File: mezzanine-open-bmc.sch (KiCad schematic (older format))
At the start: 14 parts, among them CON1 USB-MINI-B, P1 CONN_02X20, P2 CONN_02X20, SW1 PWR, SW2 RST, U1 FT230XS

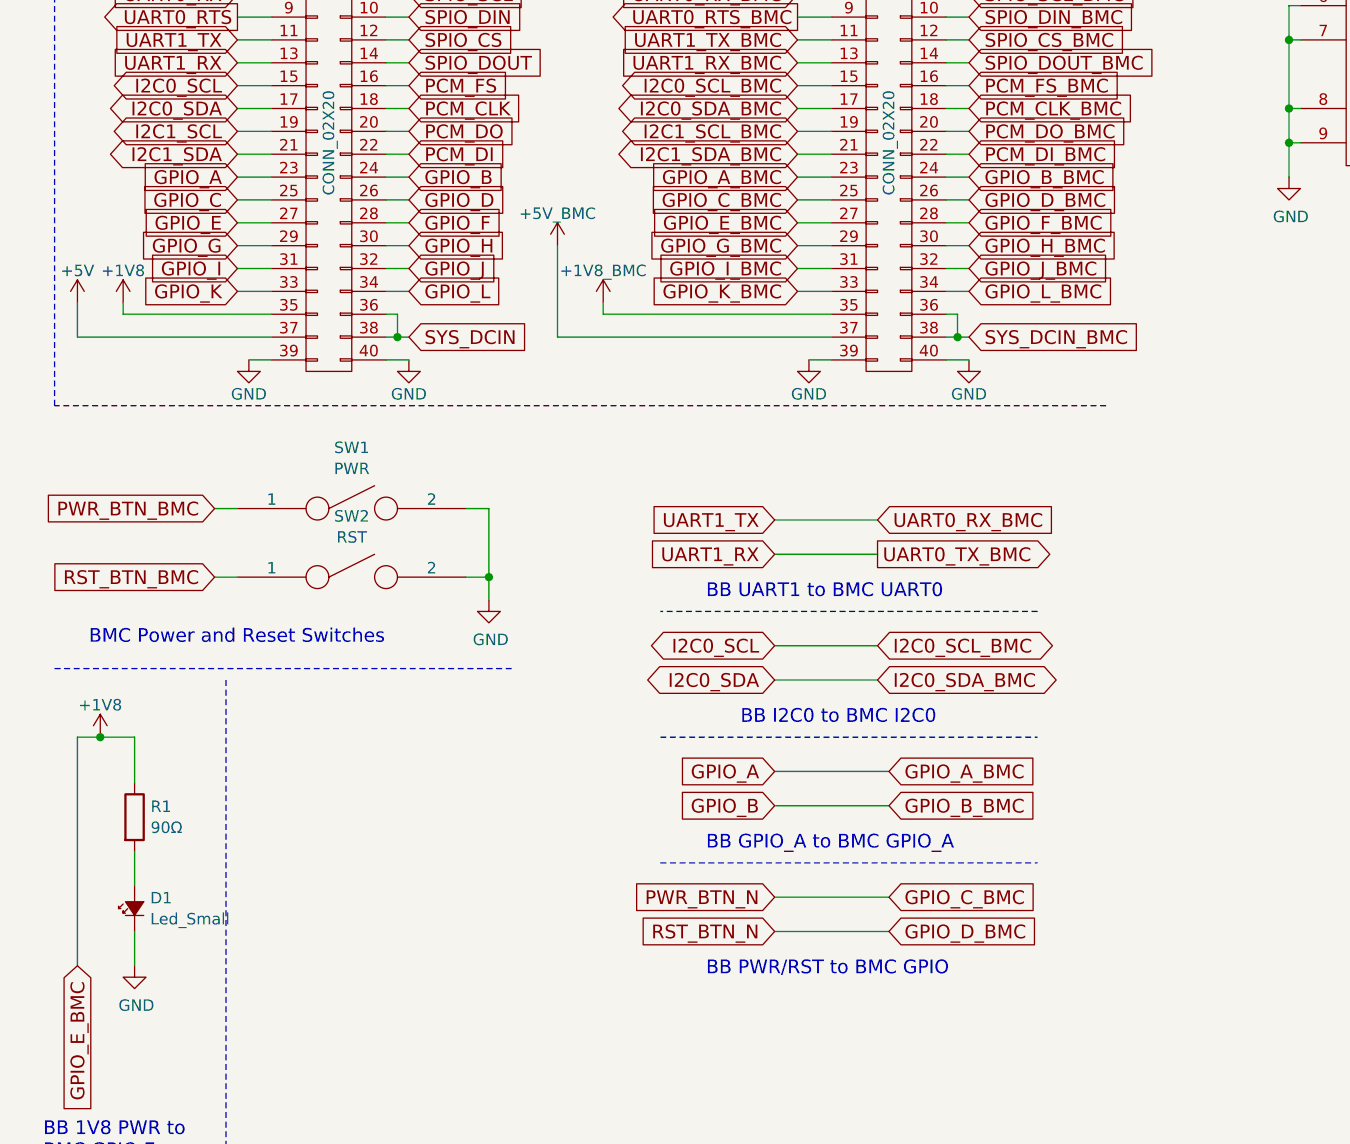
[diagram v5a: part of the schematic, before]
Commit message: Change Signal Names for GPIO_A/B BMC
Since GPIO_A and GPIO_B are to be connected on the BB & BMC pins,
the signal names have been renamed to match.

Signed-off-by: Sophie Haynes <sophie.haynes@linaro.org>
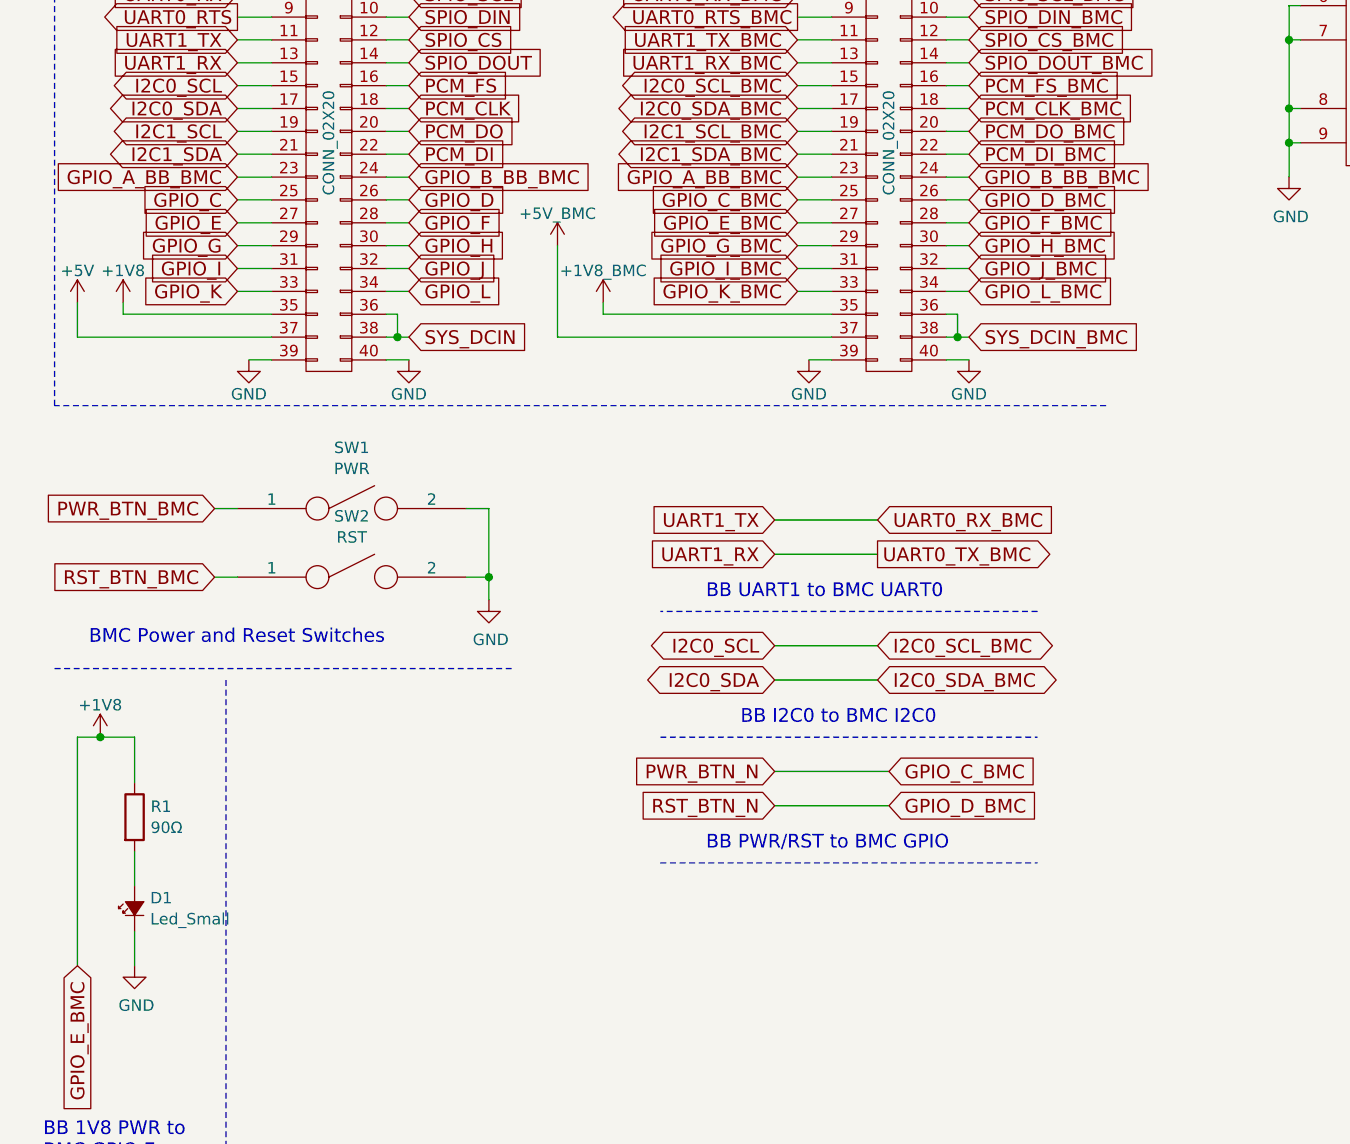
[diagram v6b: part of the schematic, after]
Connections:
- net GPIO_A renamed GPIO_A_BB_BMC
- net GPIO_B renamed GPIO_B_BB_BMC
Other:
- note removed: "BB GPIO_A to BMC GPIO_A"
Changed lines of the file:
@@
 I2C0_SCL_BMC
 Text GLabel 3950 2200 0    60   Input ~ 0
-GPIO_A_BMC
+GPIO_A_BB_BMC
 Text GLabel 3950 1400 0    60   Input ~ 0
 UART0_RX_BMC
@@
 UART1_RX_BMC
 Text GLabel 4700 2200 2    60   Input ~ 0
-GPIO_B_BMC
+GPIO_B_BB_BMC
 Text GLabel 4700 1400 2    60   Input ~ 0
 SPIO_SCL_BMC
@@
 UART0_CTS
 Text GLabel 1500 2200 0    60   Input ~ 0
-GPIO_A
+GPIO_A_BB_BMC
 Text GLabel 2250 2200 2    60   Input ~ 0
-GPIO_B
+GPIO_B_BB_BMC
 Text GLabel 1500 1600 0    60   Input ~ 0
 UART1_TX
@@
 Text Notes 3700 4600 0    60   ~ 0
 BB I2C0 to BMC I2C0
+Text GLabel 4350 4800 2    60   Input ~ 0
+GPIO_C_BMC
 Text GLabel 3850 4800 0    60   Input ~ 0
-GPIO_A
+PWR_BTN_N
 Text GLabel 3850 4950 0    60   Input ~ 0
-GPIO_B
-Text GLabel 4350 4800 2    60   Input ~ 0
-GPIO_A_BMC
+RST_BTN_N
 Text GLabel 4350 4950 2    60   Input ~ 0
-GPIO_B_BMC
+GPIO_D_BMC
 Text Notes 3550 5150 0    60   ~ 0
-BB GPIO_A to BMC GPIO_A
-Text GLabel 4350 5350 2    60   Input ~ 0
-GPIO_C_BMC
-Text GLabel 3850 5350 0    60   Input ~ 0
-PWR_BTN_N
-Text GLabel 3850 5500 0    60   Input ~ 0
-RST_BTN_N
-Text GLabel 4350 5500 2    60   Input ~ 0
-GPIO_D_BMC
-Text Notes 3550 5700 0    60   ~ 0
 BB PWR/RST to BMC GPIO
 $Comp
@@
 Wire Notes Line
 	5000 4100 3350 4100
-Wire Wire Line
-	3850 4800 4350 4800
-Wire Wire Line
-	4350 4950 3850 4950
 Wire Notes Line
 	3350 4650 5000 4650
@@
 	3350 5200 5000 5200
 Wire Wire Line
-	4350 5350 3850 5350
-Wire Wire Line
-	3850 5500 4350 5500
+	4350 4800 3850 4800
+Wire Wire Line
+	3850 4950 4350 4950
 Wire Wire Line
 	2900 2900 2900 2500

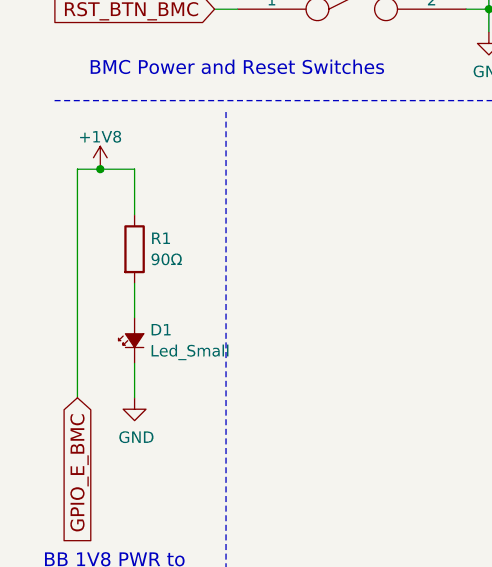
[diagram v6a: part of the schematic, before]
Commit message: Add 22R to GPIO_B_BMC, Add to BMC Lib
To protect the board, a resistor has been added to the GPIO line

Signed-off-by: Sophie Haynes <sophie.haynes@linaro.org>
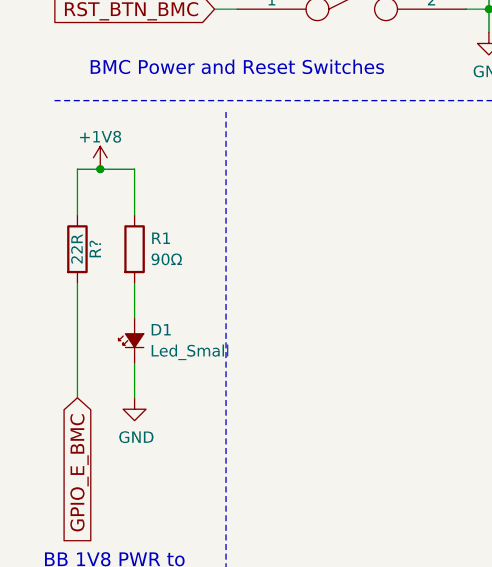
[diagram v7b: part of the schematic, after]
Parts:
- added R?: 22R, symbol R
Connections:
- net +1V8: now also R?.1; no longer P2.27 (P27)
- new net GPIO_E_BMC: P2.27 (P27), R?.2
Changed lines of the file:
@@
 	2900 2900 2900 2500
-Wire Wire Line
-	800  5650 800  4650
 Wire Wire Line
 	800  4650 1050 4650
@@
 	0    1    1    0
 $EndComp
+$Comp
+L R R?
+U 1 1 56E144A3
+P 800 5000
+F 0 "R?" V 880 5000 50  0000 C CNN
+F 1 "22R" V 800 5000 50  0000 C CNN
+F 2 "" V 730 5000 50  0000 C CNN
+F 3 "" H 800 5000 50  0000 C CNN
+	1    800  5000
+	1    0    0    -1
+$EndComp
+Wire Wire Line
+	800  4650 800  4850
+Wire Wire Line
+	800  5150 800  5650
 $EndSCHEMATC

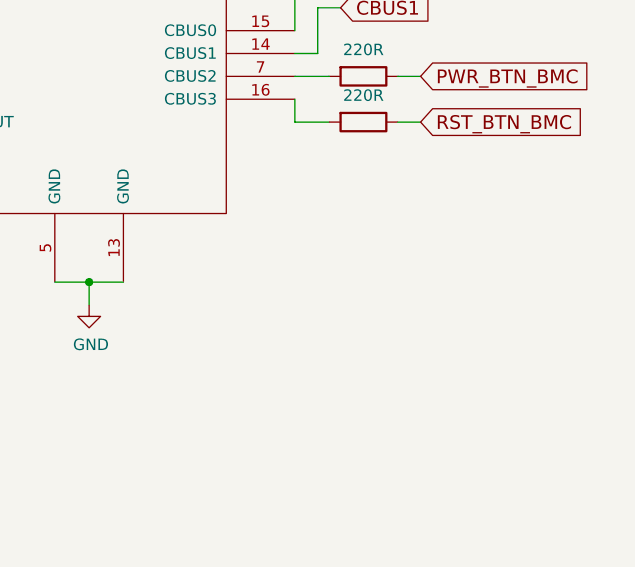
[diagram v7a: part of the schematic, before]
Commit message: Add Decoupling Caps to FTDI
Decoupling capacitors were missing from the schematic. These have been added
(including footprints).

Signed-off-by: Sophie Haynes <sophie.haynes@linaro.org>
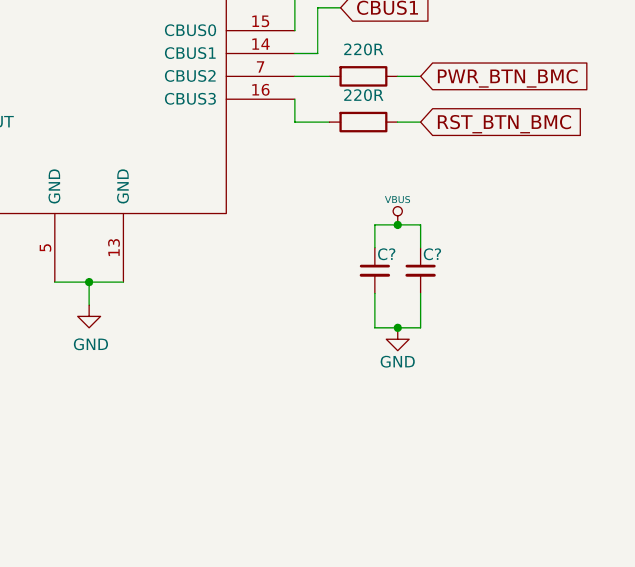
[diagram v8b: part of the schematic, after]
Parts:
- added C?: 1uF, Capacitors_SMD:C_0603, symbol C_Small
- added C?: 100nF, Capacitors_SMD:C_0603, symbol C_Small
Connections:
- net +3V3: now also C?.2, C?.2
- net VBUS: now also C?.1, C?.1
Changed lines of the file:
@@
 Wire Wire Line
 	800  5150 800  5650
+$Comp
+L VBUS #PWR?
+U 1 1 56E1B199
+P 10400 2950
+F 0 "#PWR?" H 10400 3050 30  0001 C CNN
+F 1 "VBUS" H 10400 3060 30  0000 C CNN
+F 2 "" H 10400 2950 60  0000 C CNN
+F 3 "" H 10400 2950 60  0000 C CNN
+	1    10400 2950
+	1    0    0    -1
+$EndComp
+$Comp
+L C_Small C?
+U 1 1 56E1B1C8
+P 10300 3150
+F 0 "C?" H 10310 3220 50  0000 L CNN
+F 1 "1uF" H 10310 3070 50  0001 L CNN
+F 2 "Capacitors_SMD:C_0603" H 10300 3150 50  0001 C CNN
+F 3 "" H 10300 3150 50  0000 C CNN
+	1    10300 3150
+	1    0    0    -1
+$EndComp
+$Comp
+L C_Small C?
+U 1 1 56E1B202
+P 10500 3150
+F 0 "C?" H 10510 3220 50  0000 L CNN
+F 1 "100nF" H 10510 3070 50  0001 L CNN
+F 2 "Capacitors_SMD:C_0603" H 10500 3150 50  0001 C CNN
+F 3 "" H 10500 3150 50  0000 C CNN
+	1    10500 3150
+	1    0    0    -1
+$EndComp
+Wire Wire Line
+	10300 3050 10300 2950
+Wire Wire Line
+	10300 2950 10500 2950
+Wire Wire Line
+	10500 2950 10500 3050
+Connection ~ 10400 2950
+$Comp
+L GND #PWR?
+U 1 1 56E1B3A1
+P 10400 3400
+F 0 "#PWR?" H 10400 3150 50  0001 C CNN
+F 1 "GND" H 10400 3250 50  0000 C CNN
+F 2 "" H 10400 3400 50  0000 C CNN
+F 3 "" H 10400 3400 50  0000 C CNN
+	1    10400 3400
+	1    0    0    -1
+$EndComp
+Wire Wire Line
+	10300 3400 10500 3400
+Wire Wire Line
+	10300 3400 10300 3250
+Wire Wire Line
+	10500 3400 10500 3250
+Connection ~ 10400 3400
 $EndSCHEMATC
